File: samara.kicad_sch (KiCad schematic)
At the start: 55 parts, among them J1 CONN_02JST-PTH-2, J2 U.FL, J3 I2C_STANDARDQWIIC, P1 USB_C_Plug_USB2.0, Q1 DMG3418L, U1 RP2040, U2 BNO055, U3 BME280, U4 W25Q16JVSNIQ, U5 RFM95W-915S2, U6 MCP73831, U7 AP2112K-3.3, Y1 CRYSTAL-12MHZ", Y2 CRYSTAL-32.768KHZSMD-3.2X1.5

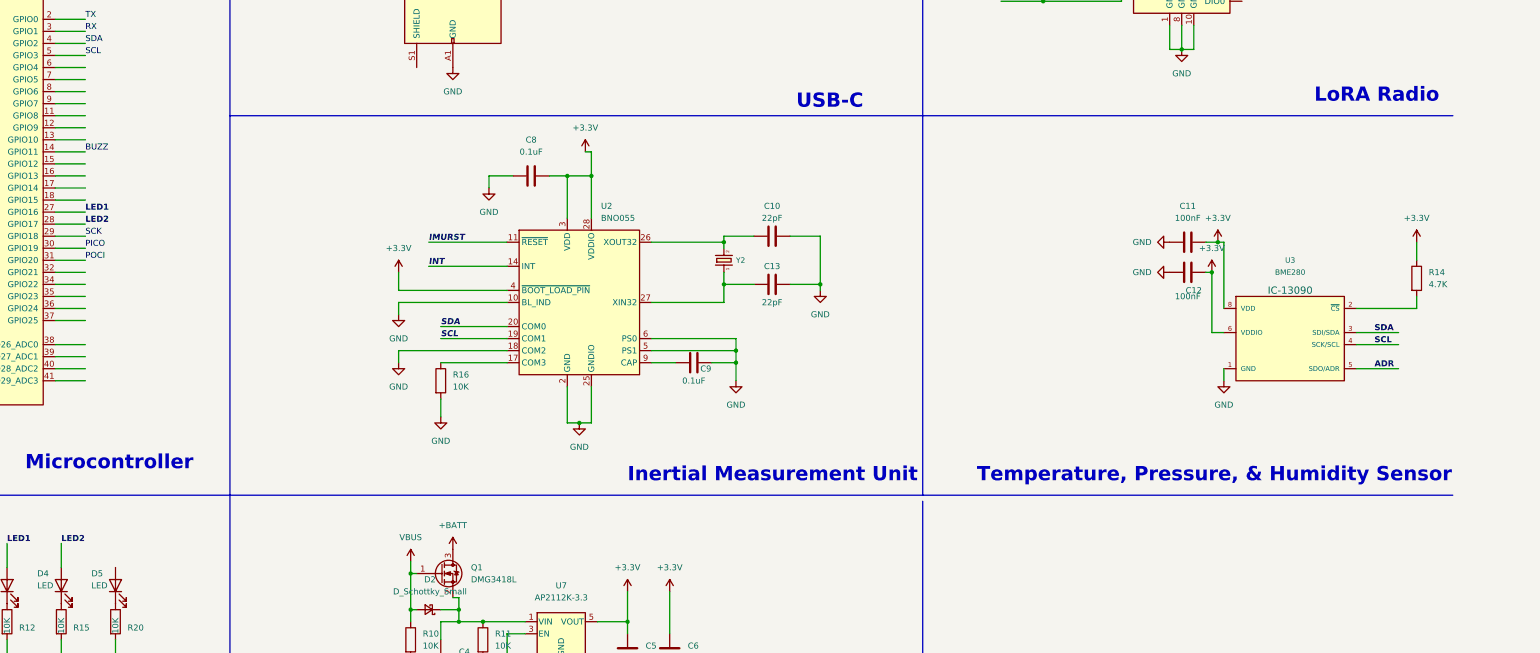
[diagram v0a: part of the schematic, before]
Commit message: updated IMU to BMI085
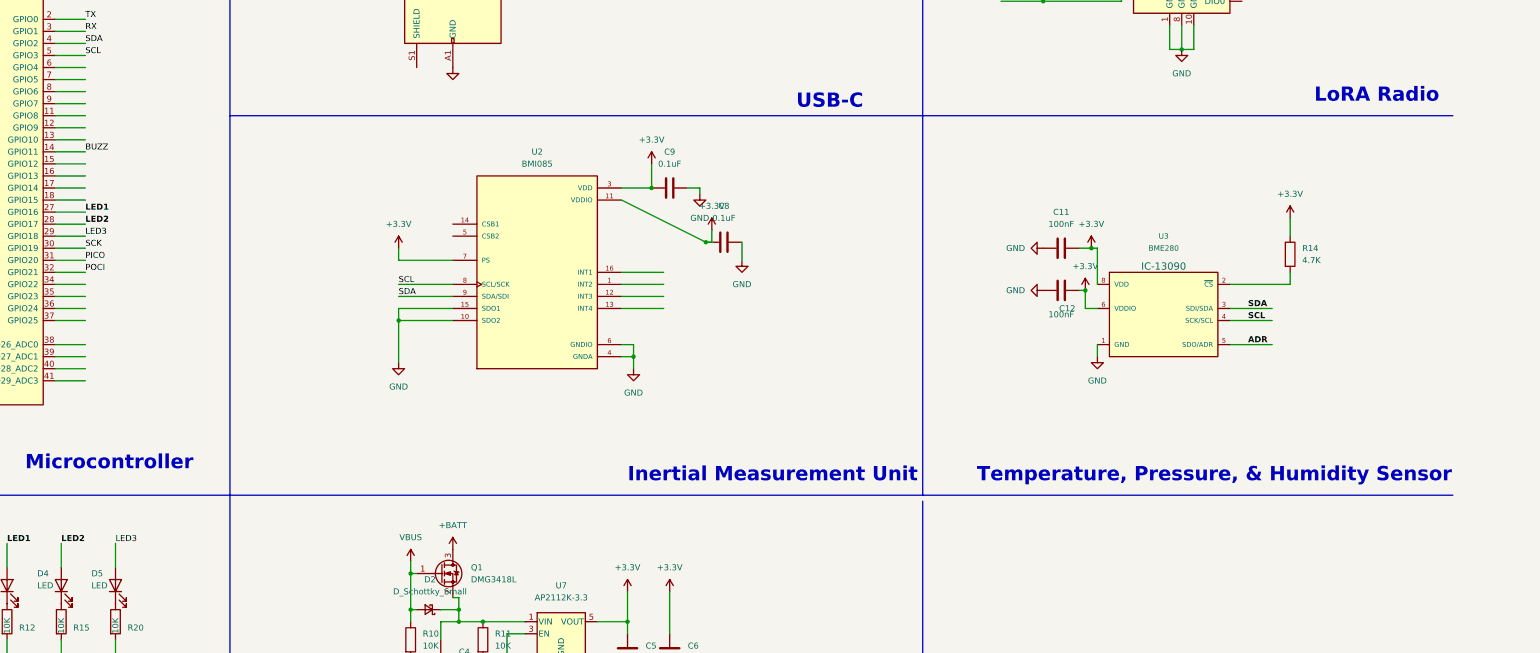
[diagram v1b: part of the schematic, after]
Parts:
- removed C10, C13: 22pF, Capacitor_SMD:C_0402_1005Metric, symbol Device:C
- removed R16: 10K, Resistor_SMD:R_0402_1005Metric, symbol Device:R
- removed U2: BNO055, Package_LGA:LGA-28_5.2x3.8mm_P0.5mm, symbol Sensor_Motion:BNO055
- removed Y2: CRYSTAL-32.768KHZSMD-3.2X1.5, CRYSTAL-SMD-3.2X1.5MM, symbol SparkFun-Clocks:CRYSTAL-32.768KHZSMD-3.2X1.5
- added U2: BMI085, PQFN50P450X300X100-16N, symbol BMI085:BMI085
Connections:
- net +3V3: now also C8.1, C9.1, U2.11 (VDDIO), U2.3 (VDD), U2.7 (PS); no longer C8.2
- net GND: now also C8.2, U2.10 (SDO2), U2.15 (SDO1), U2.4 (GNDA), U2.6 (GNDIO); no longer C8.1
- net PICO: now also U1.31 (GPIO20); no longer U1.30 (GPIO19)
- net POCI: now also U1.32 (GPIO21); no longer U1.31 (GPIO20)
- net SCK: now also U1.30 (GPIO19); no longer U1.29 (GPIO18)
- net SCL: now also U2.8 (SCL/SCK)
- net SDA: now also U2.9 (SDA/SDI)
- net LED3: now reaches D5.2 (A)
- net LED3: now also U1.29 (GPIO18)
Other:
- moved on the sheet: C11, C12, C8, R14, U3

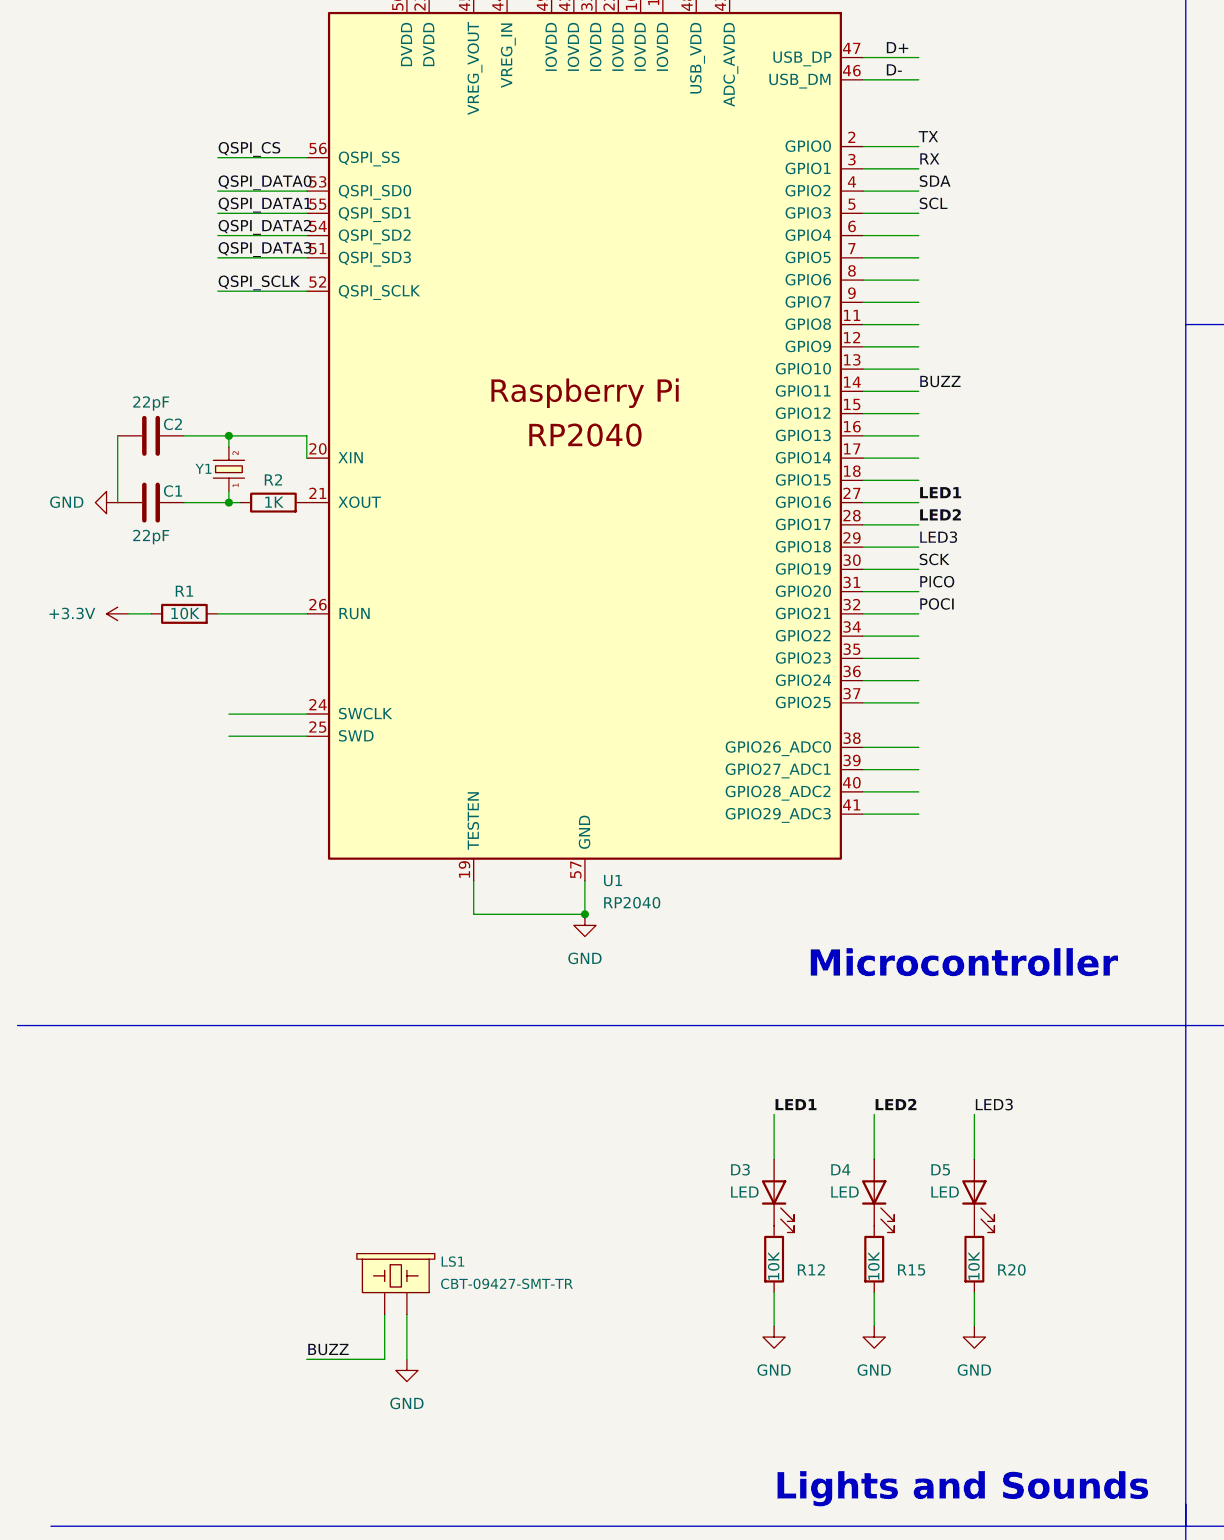
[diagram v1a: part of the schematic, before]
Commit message: update 3d models
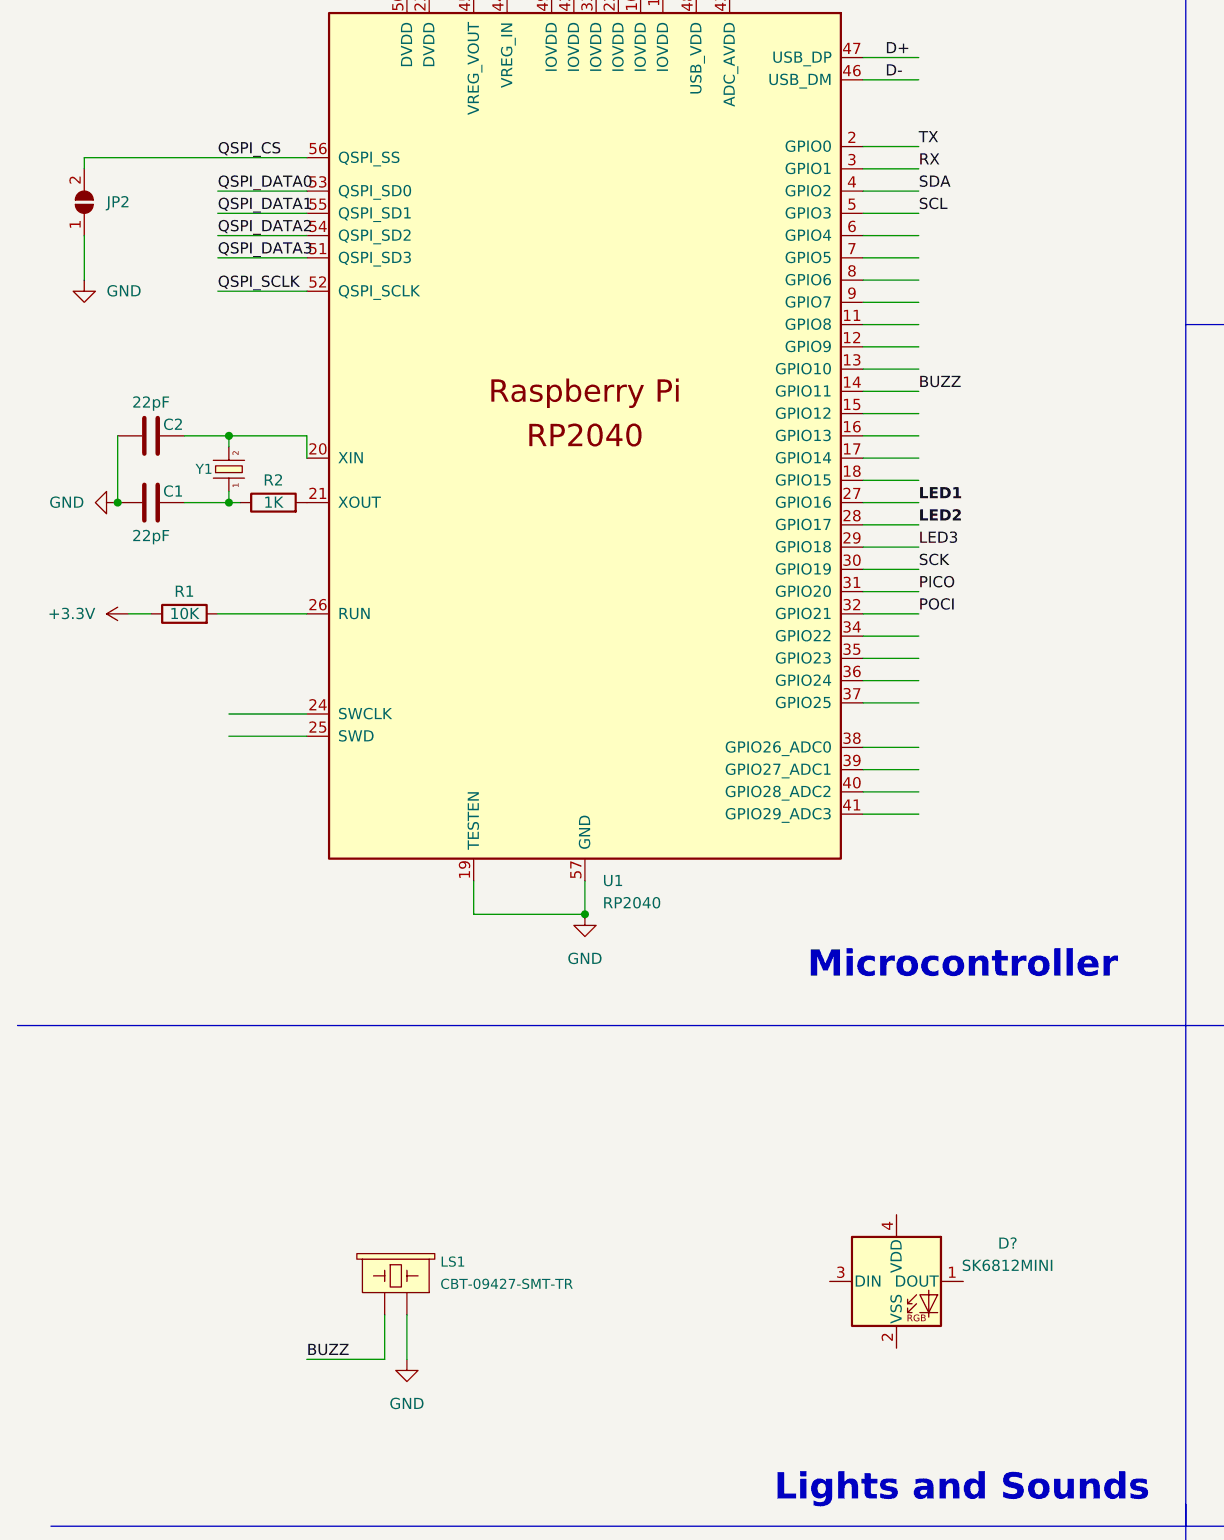
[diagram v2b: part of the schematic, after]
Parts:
- removed D3, D4, D5: LED, LED_SMD:LED_0603_1608Metric, symbol Device:LED
- removed R12, R15, R20: 10K, Resistor_SMD:R_0402_1005Metric, symbol Device:R
- added D?: SK6812MINI, LED_SMD:LED_SK6812MINI_PLCC4_3.5x3.5mm_P1.75mm, symbol LED:SK6812MINI
- added JP2: SolderJumper_2_Open, Jumpers:SMT-JUMPER_2_NO_NO-SILK, symbol Jumper:SolderJumper_2_Open
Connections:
- net GND: now also JP2.1 (A)
- net QSPI_CS: now also JP2.2 (B)

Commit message: assorted updates and 3d models
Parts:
- removed D?: SK6812MINI, LED_SMD:LED_SK6812MINI_PLCC4_3.5x3.5mm_P1.75mm, symbol LED:SK6812MINI
- added D3: SK6805, LED_SMD:LED_SK6805_PLCC4_2.4x2.7mm_P1.3mm, symbol LED:SK6805
- added J4: CONN_01, Connectors:1X01_NO_SILK, symbol SparkFun-Connectors:CONN_01
- added J5: CONN_02, 1X02, symbol SparkFun-Connectors:CONN_02
- U7: value AP2112K-3.3 -> LDS3985M33R
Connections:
- net +3V3: now also D3.4 (VDD)
- net GND: now also J2.1 (GND), J2.2 (GND), D3.2 (VSS), J5.1
- net LED1: now also D3.3 (DIN)
- net at R1.2, U1.26 (RUN): now also J5.2
- net at J2.FEED (SIGNAL), U5.9 (ANT): now also J4.1
- net LED2: no longer names the net of U1.28 (GPIO17)
- net LED3: no longer names the net of U1.29 (GPIO18)
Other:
- note added: "Double check this"
- note removed: "Add a switch here"

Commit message: close to v1 production
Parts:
- removed J2: U.FL, Connectors:U.FL, symbol SparkFun-Connectors:U.FL
- removed J4: CONN_01, Connectors:1X01_NO_SILK, symbol SparkFun-Connectors:CONN_01
- added J2: CON-SMA-EDGE-S, RFSOLUTIONS_CON-SMA-EDGE-S, symbol CON-SMA-EDGE-S:CON-SMA-EDGE-S
- added J4: U.FL, U.FL, symbol SparkFun-Connectors:U.FL
- added J6: CONN_03, 1X03, symbol SparkFun-Connectors:CONN_03
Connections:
- net GND: now also J2.G1, J2.G2, J2.G3, J2.G4, J4.1 (GND), J4.2 (GND), J6.1
- net RX: now also J6.2
- net TX: now also J6.3
- net at U5.9 (ANT): now also J2.1, J4.FEED (SIGNAL)
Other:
- note added: "BREAKOUT RX/TX to headers"

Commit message: ready for first pcb fab
get ready for bodges...
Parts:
- added C10, C13, C14, C15, C16, C18, C19, C20, C21: 0.1uF, Capacitor_SMD:C_0402_1005Metric, symbol Device:C
- added C17, C22, C23: 2.2uF, Capacitor_SMD:C_0402_1005Metric, symbol Device:C
- added R12: 10K, Resistor_SMD:R_0402_1005Metric, symbol Device:R
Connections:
- net +3V3: now also C10.2, C14.2, C16.2, C18.2, C19.2, C20.2, C21.2, C22.2, R12.1; no longer U1.43 (ADC_AVDD)
- net GND: now also JP2.2 (B), C10.1, C13.1, C14.1, C15.1, C16.1, C17.1, C18.1, C19.1, C20.1, C21.1, C22.1, C23.1; no longer JP2.1 (A)
- net NSS: now also U1.29 (GPIO18)
- net QSPI_CS: now also JP2.1 (A); no longer JP2.2 (B)
- net RST: now also U1.28 (GPIO17)
- net +1V2: now reaches U1.23 (DVDD)
- net +1V2: now also U1.45 (VREG_VOUT), C13.2, C15.2, C17.2
- new net: C23.2, R12.2, U1.43 (ADC_AVDD)
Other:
- note removed: "BREAKOUT RX/TX to headers"
- note removed: "Double check this"
- moved on the sheet: C8, D3, J5, JP2, R7
